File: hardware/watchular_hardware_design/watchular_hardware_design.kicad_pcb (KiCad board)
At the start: 4 copper layers, 54 x 22.9 mm, 90 parts, among them J1 USB4105-GF-A, J2 665102131822, J3 TSW-116-07-H-S, J4 TSW-116-07-H-S, Q1 BSS123, Q2 BSS123, Q3 BSS123, Q4 BSS123, T1 DMG1013UW-7, U1 MCP73832T-2DCI/OT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

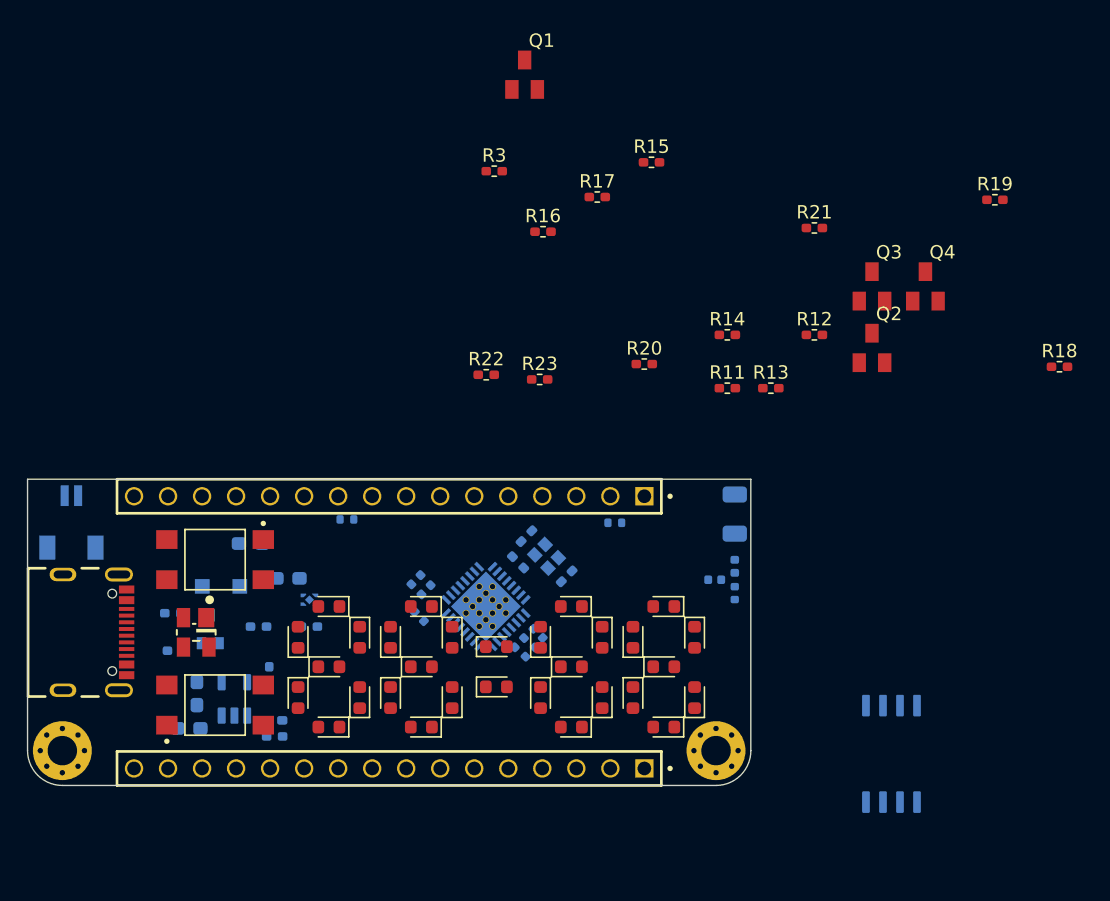
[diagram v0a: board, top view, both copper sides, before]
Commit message: Made all 4 corners rounded.
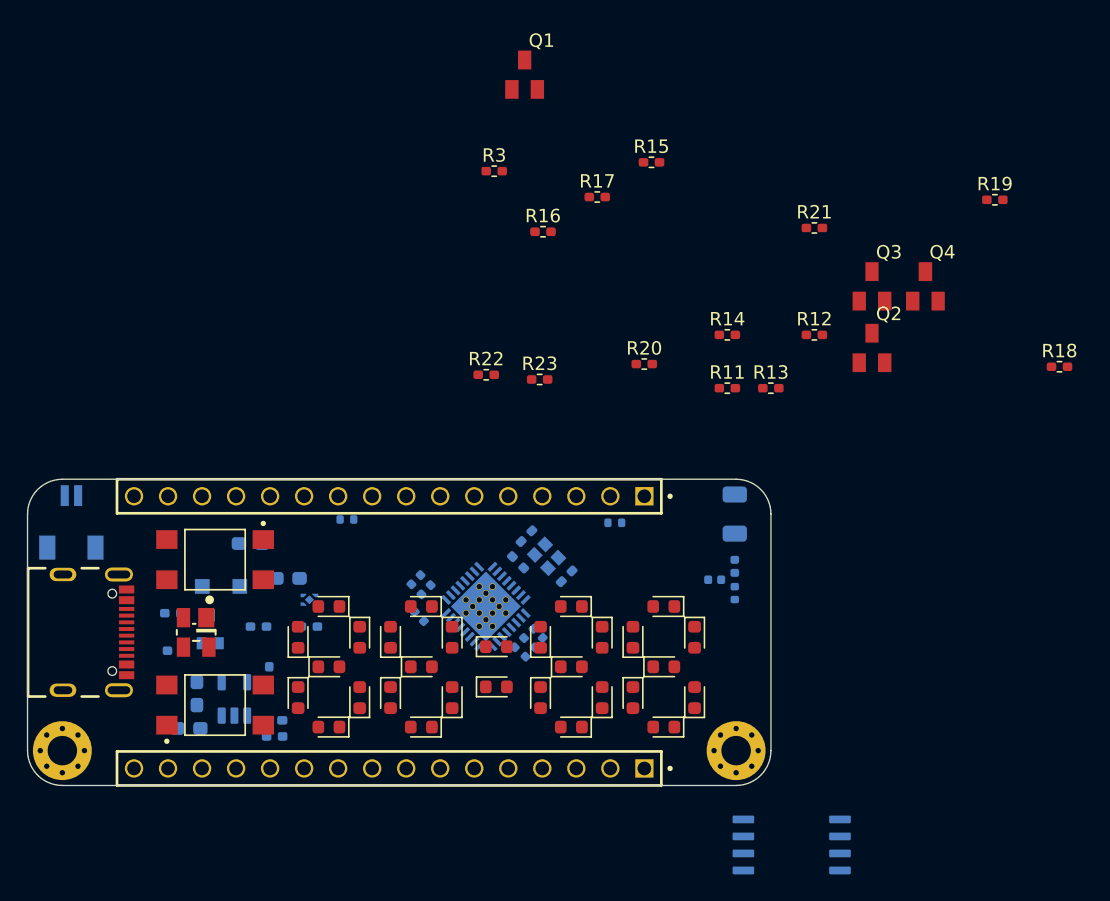
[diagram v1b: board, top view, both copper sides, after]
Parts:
- moved U4 10.1 mm to (147.1, 137.3), turned to 180 degrees
- moved H1 1.50 mm to (142.9, 130.3)
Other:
- board size 54 x 22.9 mm -> 55.5 x 22.9 mm
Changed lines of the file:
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@@
     )
   )
-  (footprint "MountingHole:MountingHole_2.2mm_M2_Pad_Via" (layer "F.Cu")
-    (at 141.4 130.26)
+  (footprint "MountingHole:MountingHole_2.2mm_M2_Pad_Via" locked (layer "F.Cu")
+    (at 142.9 130.26)
     (descr "Mounting Hole 2.2mm, M2")
     (tags "mounting hole 2.2mm m2")
@@
     (fp_circle (center 0 0) (end 2.2 0) (layer "Cmts.User") (width 0.15) (fill none))
     (fp_circle (center 0 0) (end 2.45 0) (layer "F.CrtYd") (width 0.05) (fill none))
-    (pad "1" thru_hole circle (at 0 0) (size 4.4 4.4) (drill 2.2) (layers *.Cu *.Mask)
+    (pad "1" thru_hole circle locked (at 0 0) (size 4.4 4.4) (drill 2.2) (layers *.Cu *.Mask)
       (net 4 "GND") (pinfunction "1") (pintype "input"))
-    (pad "1" thru_hole circle (at -1.65 0) (size 0.7 0.7) (drill 0.4) (layers *.Cu *.Mask)
+    (pad "1" thru_hole circle locked (at -1.65 0) (size 0.7 0.7) (drill 0.4) (layers *.Cu *.Mask)
       (net 4 "GND") (pinfunction "1") (pintype "input"))
-    (pad "1" thru_hole circle (at -1.166726 -1.166726) (size 0.7 0.7) (drill 0.4) (layers *.Cu *.Mask)
+    (pad "1" thru_hole circle locked (at -1.166726 -1.166726) (size 0.7 0.7) (drill 0.4) (layers *.Cu *.Mask)
       (net 4 "GND") (pinfunction "1") (pintype "input"))
-    (pad "1" thru_hole circle (at 0 1.65) (size 0.7 0.7) (drill 0.4) (layers *.Cu *.Mask)
+    (pad "1" thru_hole circle locked (at 0 1.65) (size 0.7 0.7) (drill 0.4) (layers *.Cu *.Mask)
       (net 4 "GND") (pinfunction "1") (pintype "input"))
-    (pad "1" thru_hole circle (at 1.65 0) (size 0.7 0.7) (drill 0.4) (layers *.Cu *.Mask)
+    (pad "1" thru_hole circle locked (at 1.65 0) (size 0.7 0.7) (drill 0.4) (layers *.Cu *.Mask)
       (net 4 "GND") (pinfunction "1") (pintype "input"))
-    (pad "1" thru_hole circle (at -1.166726 1.166726) (size 0.7 0.7) (drill 0.4) (layers *.Cu *.Mask)
+    (pad "1" thru_hole circle locked (at -1.166726 1.166726) (size 0.7 0.7) (drill 0.4) (layers *.Cu *.Mask)
       (net 4 "GND") (pinfunction "1") (pintype "input"))
-    (pad "1" thru_hole circle (at 0 -1.65) (size 0.7 0.7) (drill 0.4) (layers *.Cu *.Mask)
+    (pad "1" thru_hole circle locked (at 0 -1.65) (size 0.7 0.7) (drill 0.4) (layers *.Cu *.Mask)
       (net 4 "GND") (pinfunction "1") (pintype "input"))
-    (pad "1" thru_hole circle (at 1.166726 -1.166726) (size 0.7 0.7) (drill 0.4) (layers *.Cu *.Mask)
+    (pad "1" thru_hole circle locked (at 1.166726 -1.166726) (size 0.7 0.7) (drill 0.4) (layers *.Cu *.Mask)
       (net 4 "GND") (pinfunction "1") (pintype "input"))
-    (pad "1" thru_hole circle (at 1.166726 1.166726) (size 0.7 0.7) (drill 0.4) (layers *.Cu *.Mask)
+    (pad "1" thru_hole circle locked (at 1.166726 1.166726) (size 0.7 0.7) (drill 0.4) (layers *.Cu *.Mask)
       (net 4 "GND") (pinfunction "1") (pintype "input"))
   )
@@
   )
   (footprint "W25Q16JVSSIQ:SOIC127P790X216-8N" (layer "B.Cu")
-    (at 154.5 130.5 90)
+    (at 147.05 137.3 180)
     (property "AVAILABILITY" "Unavailable")
     (property "DESCRIPTION" "3v 16m-Bit Serial Flash Memory With Dual")
@@
     (property "Sheetname" "")
     (attr through_hole)
-    (fp_text reference "U4" (at -1.05616 3.50582 90) (layer "B.Fab") hide
+    (fp_text reference "U4" (at -1.05616 3.50582) (layer "B.Fab") hide
       (effects (font (size 1.001087 1.001087) (thickness 0.15)) (justify mirror))
     )
-    (fp_text value "W25Q16JVSSIQ" (at 7.21091 -3.507335 90) (layer "B.Fab") hide
+    (fp_text value "W25Q16JVSSIQ" (at 7.21091 -3.507335) (layer "B.Fab") hide
       (effects (font (size 1.00152 1.00152) (thickness 0.15)) (justify mirror))
     )
@@
     (fp_line (start -2.69 2.69) (end -2.69 -2.69) (layer "B.Fab") (width 0.127))
     (fp_circle (center -5 2) (end -4.9 2) (layer "B.Fab") (width 0.2) (fill none))
-    (pad "1" smd roundrect locked (at -3.605 1.905 90) (size 1.61 0.58) (layers "B.Cu" "B.Paste" "B.Mask") (roundrect_rratio 0.14)
+    (pad "1" smd roundrect locked (at -3.605 1.905 180) (size 1.61 0.58) (layers "B.Cu" "B.Paste" "B.Mask") (roundrect_rratio 0.14)
       (net 3 "CS-memory") (pinfunction "~{CS}") (pintype "input"))
-    (pad "2" smd roundrect locked (at -3.605 0.635 90) (size 1.61 0.58) (layers "B.Cu" "B.Paste" "B.Mask") (roundrect_rratio 0.14)
+    (pad "2" smd roundrect locked (at -3.605 0.635 180) (size 1.61 0.58) (layers "B.Cu" "B.Paste" "B.Mask") (roundrect_rratio 0.14)
       (net 7 "DO-memory") (pinfunction "DO(IO1)") (pintype "bidirectional"))
-    (pad "3" smd roundrect locked (at -3.605 -0.635 90) (size 1.61 0.58) (layers "B.Cu" "B.Paste" "B.Mask") (roundrect_rratio 0.14)
+    (pad "3" smd roundrect locked (at -3.605 -0.635 180) (size 1.61 0.58) (layers "B.Cu" "B.Paste" "B.Mask") (roundrect_rratio 0.14)
       (net 51 "unconnected-(U4-Pad3)") (pinfunction "~{WP}(IO2)") (pintype "bidirectional+no_connect"))
-    (pad "4" smd roundrect locked (at -3.605 -1.905 90) (size 1.61 0.58) (layers "B.Cu" "B.Paste" "B.Mask") (roundrect_rratio 0.14)
+    (pad "4" smd roundrect locked (at -3.605 -1.905 180) (size 1.61 0.58) (layers "B.Cu" "B.Paste" "B.Mask") (roundrect_rratio 0.14)
       (net 4 "GND") (pinfunction "GND") (pintype "power_in"))
-    (pad "5" smd roundrect locked (at 3.605 -1.905 90) (size 1.61 0.58) (layers "B.Cu" "B.Paste" "B.Mask") (roundrect_rratio 0.14)
+    (pad "5" smd roundrect locked (at 3.605 -1.905 180) (size 1.61 0.58) (layers "B.Cu" "B.Paste" "B.Mask") (roundrect_rratio 0.14)
       (net 6 "DI-memory") (pinfunction "DI(IO0)") (pintype "bidirectional"))
-    (pad "6" smd roundrect locked (at 3.605 -0.635 90) (size 1.61 0.58) (layers "B.Cu" "B.Paste" "B.Mask") (roundrect_rratio 0.14)
+    (pad "6" smd roundrect locked (at 3.605 -0.635 180) (size 1.61 0.58) (layers "B.Cu" "B.Paste" "B.Mask") (roundrect_rratio 0.14)
       (net 5 "SPICLK-memory") (pinfunction "CLK") (pintype "input"))
-    (pad "7" smd roundrect locked (at 3.605 0.635 90) (size 1.61 0.58) (layers "B.Cu" "B.Paste" "B.Mask") (roundrect_rratio 0.14)
+    (pad "7" smd roundrect locked (at 3.605 0.635 180) (size 1.61 0.58) (layers "B.Cu" "B.Paste" "B.Mask") (roundrect_rratio 0.14)
       (net 52 "unconnected-(U4-Pad7)") (pinfunction "~{HOLD/RESET}(IO3)") (pintype "bidirectional+no_connect"))
-    (pad "8" smd roundrect locked (at 3.605 1.905 90) (size 1.61 0.58) (layers "B.Cu" "B.Paste" "B.Mask") (roundrect_rratio 0.14)
+    (pad "8" smd roundrect locked (at 3.605 1.905 180) (size 1.61 0.58) (layers "B.Cu" "B.Paste" "B.Mask") (roundrect_rratio 0.14)
       (net 44 "VDD3P3_CPU") (pinfunction "VCC") (pintype "power_in"))
   )
@@
   )
   (gr_circle (center 103.594 119) (end 103.844 119) (layer "F.SilkS") (width 0.153) (fill solid))
-  (gr_line locked (start 90 110) (end 144 110) (layer "Edge.Cuts") (width 0.1))
-  (gr_arc locked (start 144 130.26) (mid 143.238478 132.098478) (end 141.4 132.86) (layer "Edge.Cuts") (width 0.1))
-  (gr_line locked (start 144 110) (end 144 130.26) (layer "Edge.Cuts") (width 0.1))
+  (gr_line locked (start 92.6 110) (end 142.9 110) (layer "Edge.Cuts") (width 0.1))
+  (gr_arc locked (start 145.5 130.26) (mid 144.738478 132.098478) (end 142.9 132.86) (layer "Edge.Cuts") (width 0.1))
+  (gr_line locked (start 145.5 112.6) (end 145.5 130.26) (layer "Edge.Cuts") (width 0.1))
   (gr_arc locked (start 92.6 132.86) (mid 90.761522 132.098478) (end 90 130.26) (layer "Edge.Cuts") (width 0.1))
-  (gr_line locked (start 92.6 132.86) (end 141.4 132.86) (layer "Edge.Cuts") (width 0.1))
-  (gr_line locked (start 90 110) (end 90 130.26) (layer "Edge.Cuts") (width 0.1))
+  (gr_arc locked (start 90 112.6) (mid 90.761522 110.761522) (end 92.6 110) (layer "Edge.Cuts") (width 0.1))
+  (gr_arc locked (start 142.9 110) (mid 144.738478 110.761522) (end 145.5 112.6) (layer "Edge.Cuts") (width 0.1))
+  (gr_line locked (start 92.6 132.86) (end 142.9 132.86) (layer "Edge.Cuts") (width 0.1))
+  (gr_line locked (start 90 112.6) (end 90 130.26) (layer "Edge.Cuts") (width 0.1))
   (zone (net 4) (net_name "GND") (layer "In1.Cu") (hatch edge 0.508)
     (connect_pads (clearance 0))

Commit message: Battery management section in place.
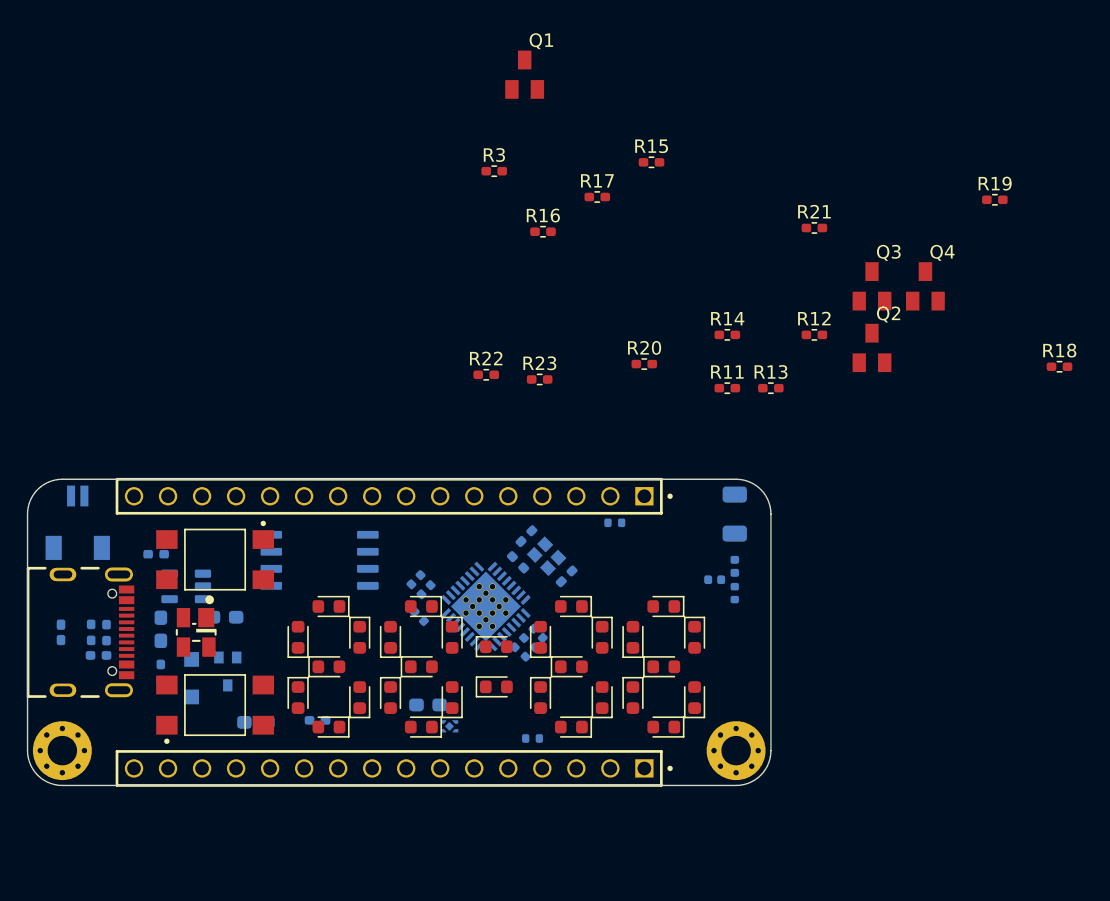
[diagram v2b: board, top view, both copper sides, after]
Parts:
- moved U4 41.2 mm to (111.8, 116.0)
- moved R9 21.4 mm to (127.7, 129.3)
- moved D1 17.2 mm to (92.5, 121.4), turned to 90 degrees
- moved R2 15.7 mm to (94.8, 121.4), turned to 90 degrees
- moved C3 14.1 mm to (119.9, 126.8)
- moved U3 14.1 mm to (121.5, 128.4)
- moved C6 13.4 mm to (107.0, 128.2)
- moved R4 12.3 mm to (99.6, 115.6), turned to 180 degrees
- moved U1 9.14 mm to (101.8, 118.0), turned to 180 degrees
- moved C2 8.72 mm to (104.7, 120.3), turned to 0 degrees
- moved R6 8.06 mm to (100.0, 124.4), turned to -90 degrees
- moved D2 7.19 mm to (102.2, 124.8), turned to 90 degrees
- moved R7 7.03 mm to (111.7, 128.0)
- moved R5 5.75 mm to (95.3, 123.2)
- moved C1 5.50 mm to (100.0, 121.2)
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
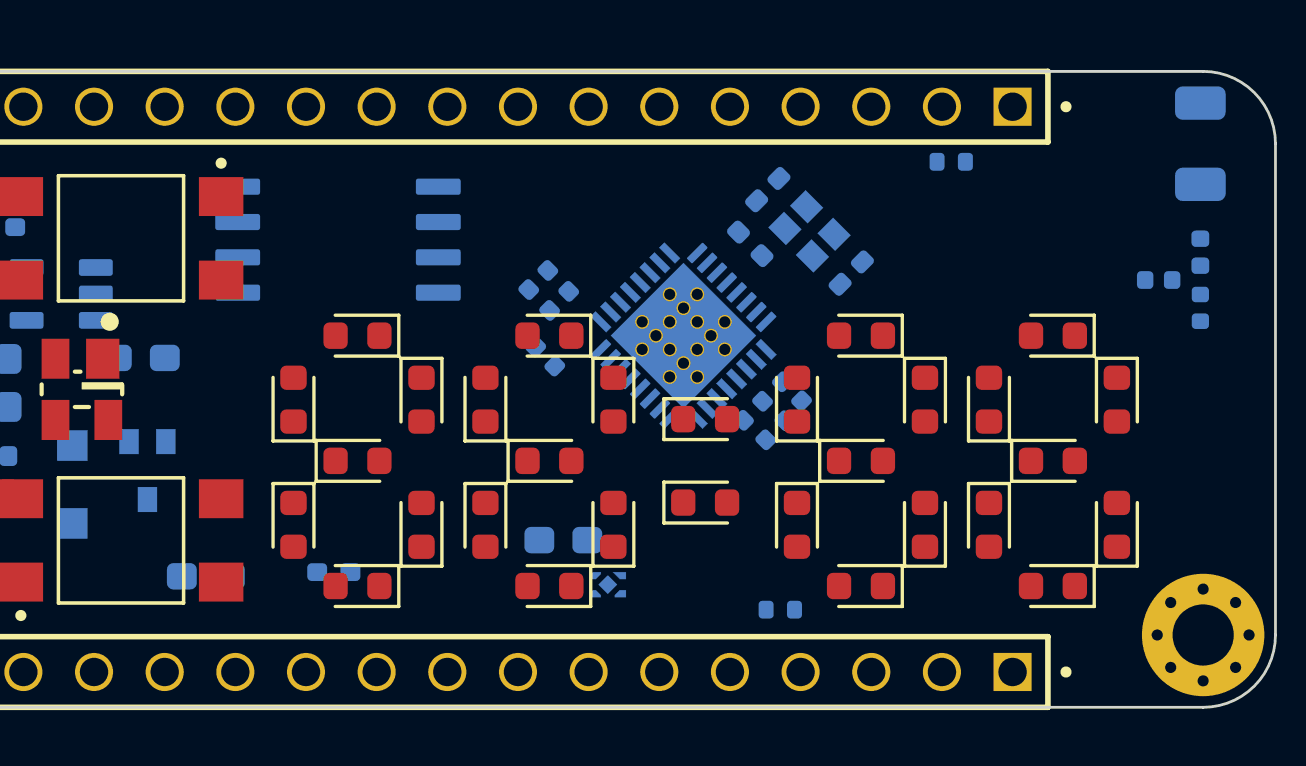
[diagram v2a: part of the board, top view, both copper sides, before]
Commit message: Moded digits to the middle.
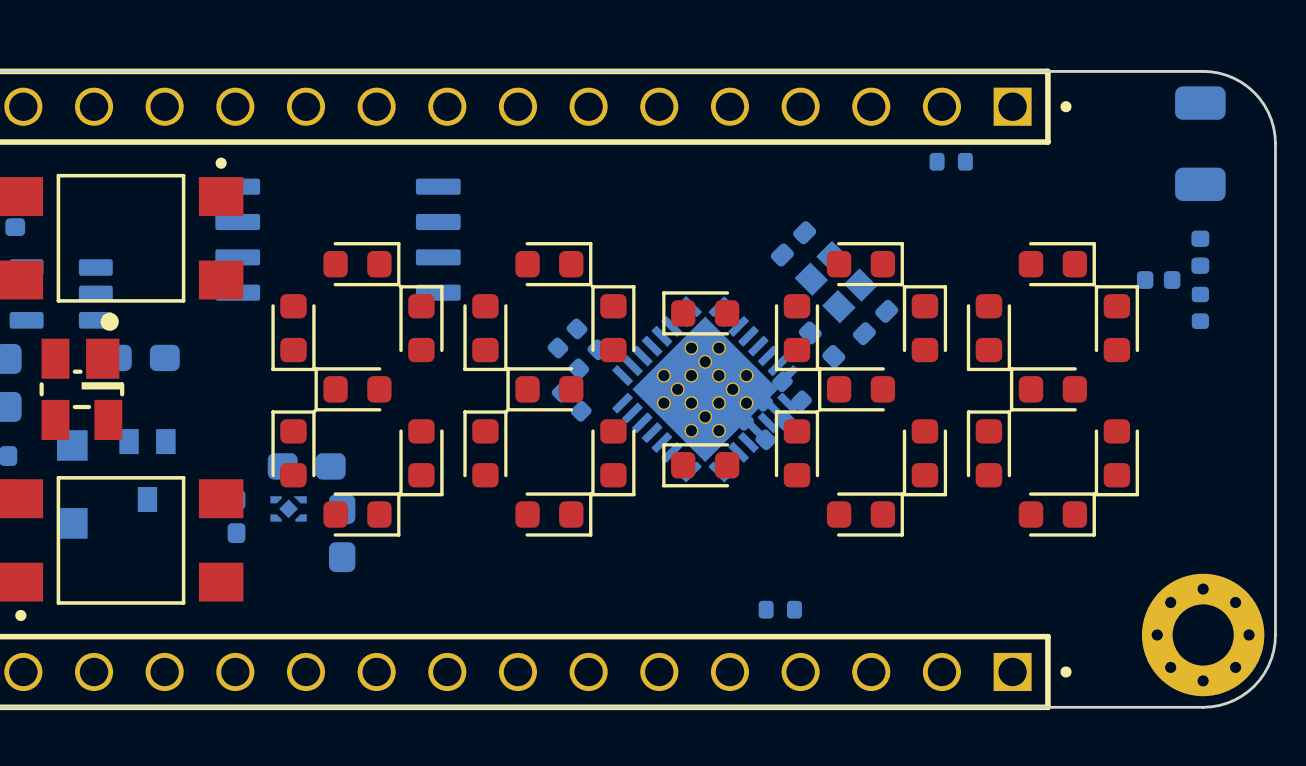
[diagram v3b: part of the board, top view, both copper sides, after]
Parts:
- moved U3 11.8 mm to (110.0, 125.7)
- moved C3 9.60 mm to (110.7, 124.2), turned to 0 degrees
- moved C5 6.15 mm to (131.1, 119.0)
- moved C6 5.14 mm to (112.0, 126.6), turned to -90 degrees
- moved R10 4.45 mm to (129.2, 119.8), turned to 135 degrees
- moved R7 4.03 mm to (108.2, 126.0), turned to -90 degrees
- moved D17 3.80 mm to (125.0, 118.7)
- moved D10 2.57 mm to (119.4, 116.9)
- moved D11 2.57 mm to (121.7, 119.2)
- moved D12 2.57 mm to (121.7, 123.7)
- moved D13 2.57 mm to (119.4, 125.9)
- moved D14 2.57 mm to (117.1, 123.7)
- moved D15 2.57 mm to (117.1, 119.2)
- moved D16 2.57 mm to (119.4, 121.4)
- moved D19 2.57 mm to (130.6, 116.9)
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- renumbered D2 to D1, D1 to D2
